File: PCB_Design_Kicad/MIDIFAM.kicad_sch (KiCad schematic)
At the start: 45 parts, among them J1 PWR_IN, J14 Conn_01x07, J15 Conn_01x07, J16 Conn_01x07, J2 ISP connector, U1 TL072, U2 MCP4822, U3 ATmega328, U4 78L05, U5 6N137

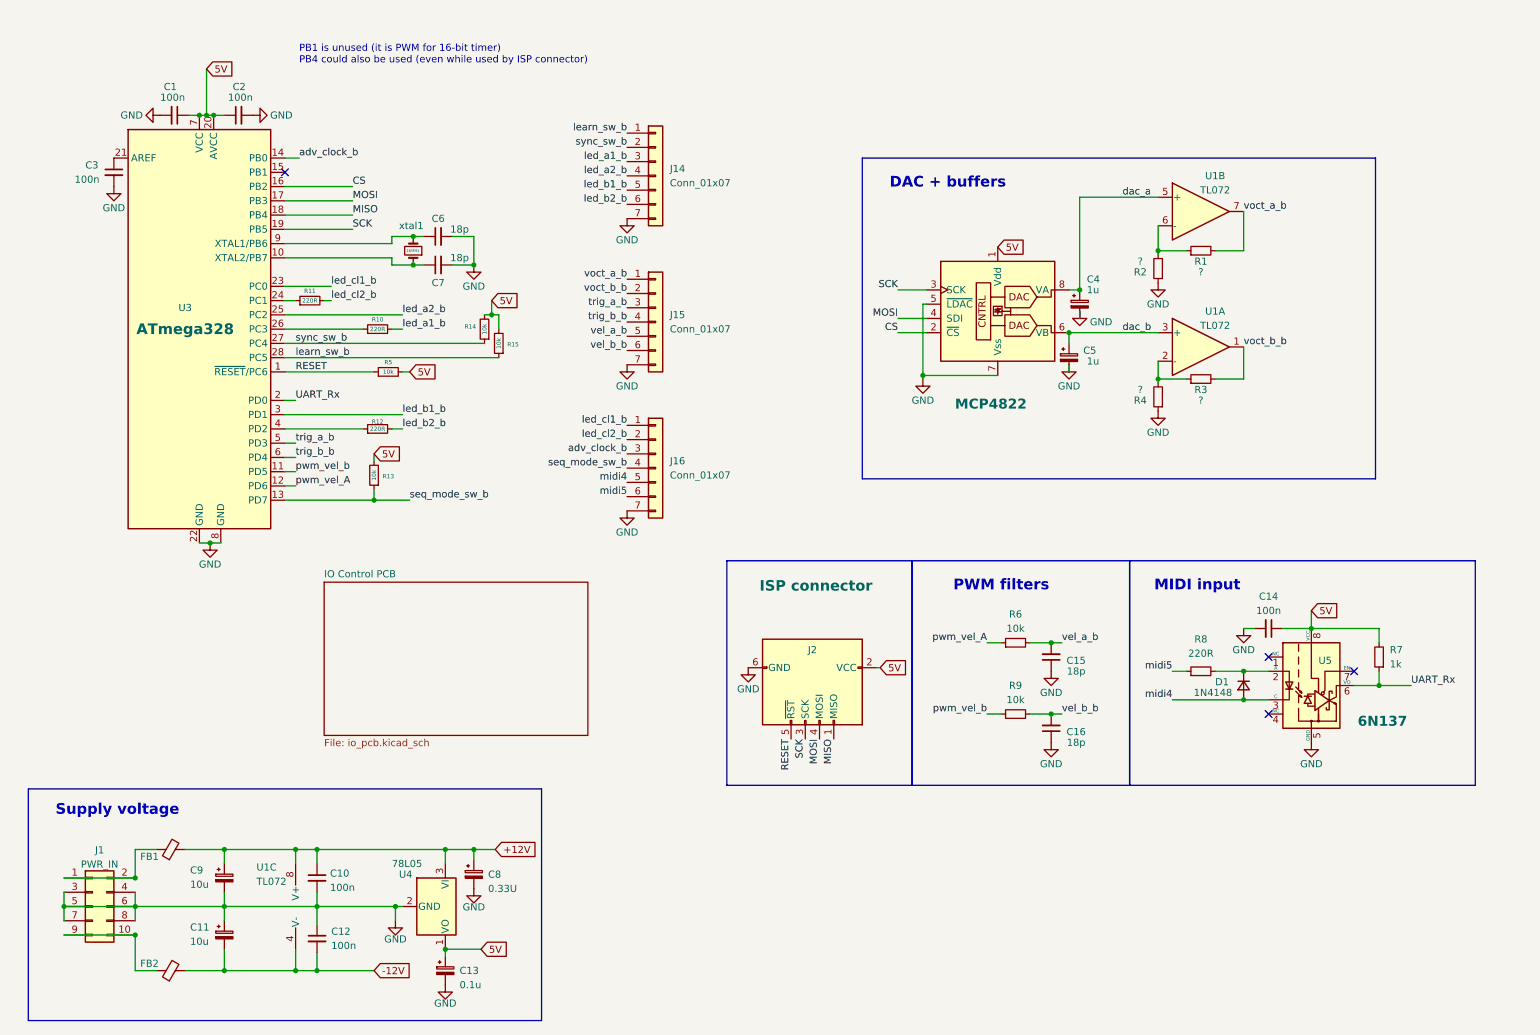
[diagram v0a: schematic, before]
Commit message: SMD pcb, routable and with vias
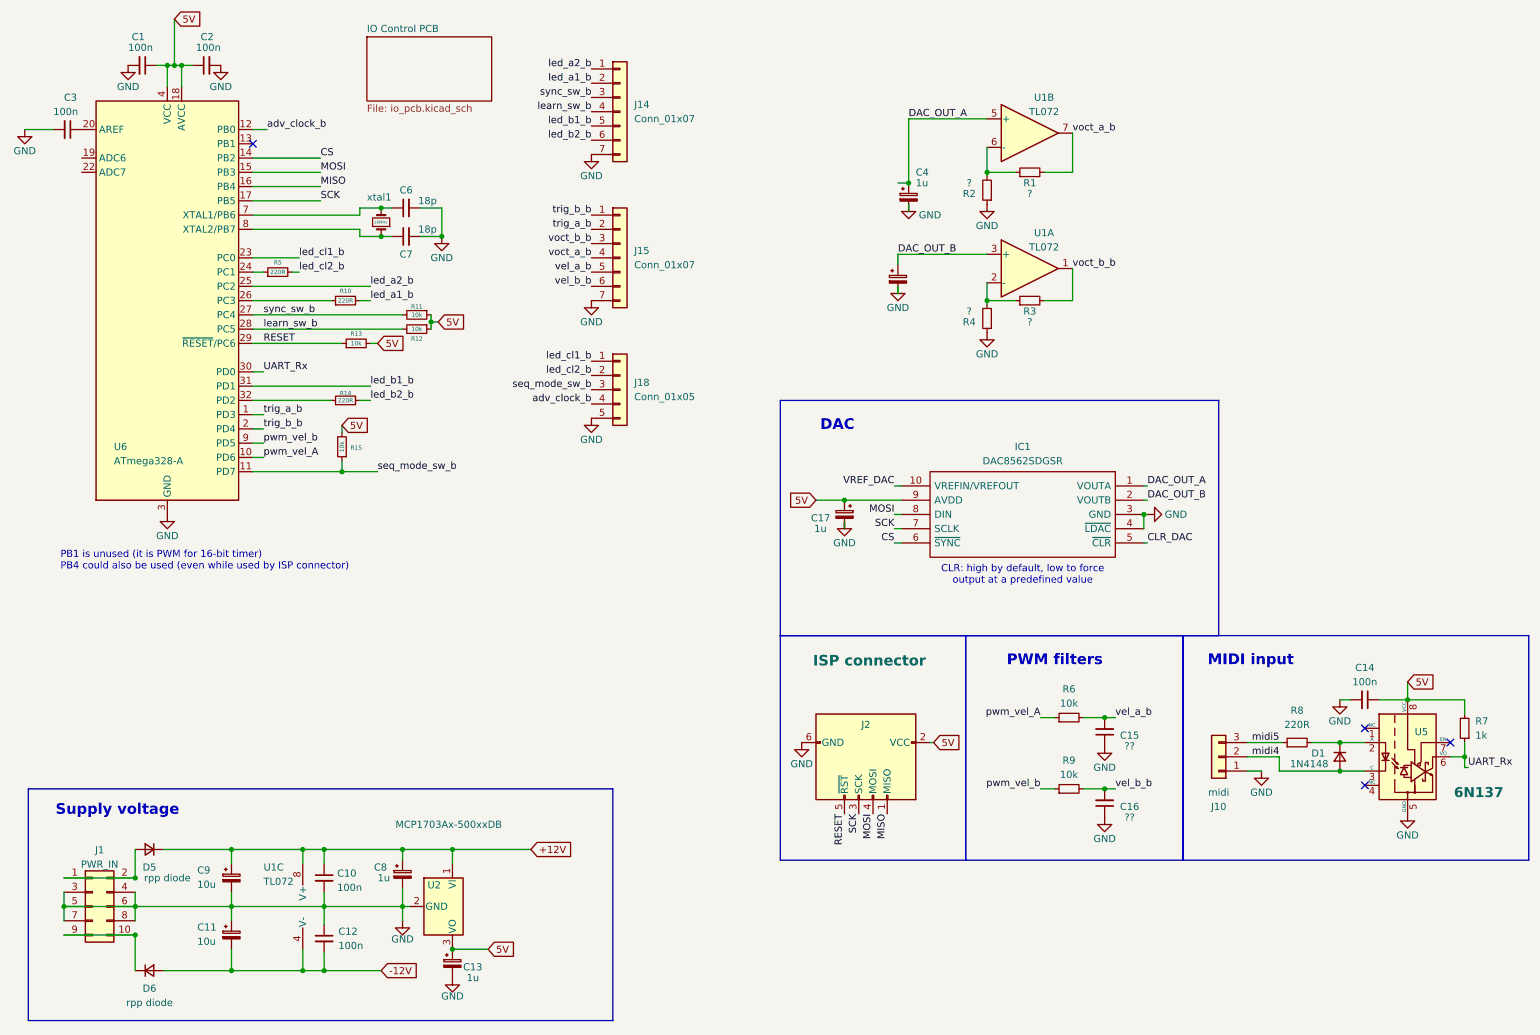
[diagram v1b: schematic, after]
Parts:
- removed FB1, FB2: FerriteBead_Small, Inductor_THT:L_Axial_L5.3mm_D2.2mm_P7.62mm_Horizontal_Vishay_IM-1, symbol Device:FerriteBead_Small
- removed J16: Conn_01x07, Connector_PinHeader_2.54mm:PinHeader_1x07_P2.54mm_Vertical, symbol Connector_Generic:Conn_01x07
- removed U2: MCP4822, Package_DIP:DIP-8_W7.62mm, symbol Analog_DAC:MCP4822
- removed U3: ATmega328, Package_DIP:DIP-28_W7.62mm, symbol MCU_Microchip_ATmega:ATmega328-P
- removed U4: 78L05, Package_TO_SOT_THT:TO-92, symbol Regulator_Linear:L78L05_TO92
- added C17: 1u, Capacitor_SMD:C_0603_1608Metric, symbol Device:C_Polarized_Small
- added D5: rpp diode, Diode_SMD:D_SOD-123F, symbol Device:D_Small
- added D6: rpp diode, Diode_SMD:D_SOD-123, symbol Device:D_Small
- added IC1: DAC8562SDGSR, SamacSys_Parts:SOP50P490X110-10N, symbol SamacSys_Parts:DAC8562SDGSR
- added J10: midi, Connector_PinHeader_2.54mm:PinHeader_1x03_P2.54mm_Vertical, symbol Connector_Generic:Conn_01x03
- added J18: Conn_01x05, Connector_PinHeader_2.54mm:PinHeader_1x05_P2.54mm_Vertical, symbol Connector_Generic:Conn_01x05
- added U2: MCP1703Ax-500xxDB, Package_TO_SOT_SMD:SOT-223-3_TabPin2, symbol Regulator_Linear:MCP1703Ax-500xxDB
- added U6: ATmega328-A, Package_QFP:TQFP-32_7x7mm_P0.8mm, symbol MCU_Microchip_ATmega:ATmega328-A
- C1, C14, C2, C3: footprint Capacitor_THT:C_Disc_D3.0mm_W2.0mm_P2.50mm -> Capacitor_SMD:C_0603_1608Metric
- C10, C12, C6, C7: footprint Capacitor_THT:C_Disc_D3.0mm_W1.6mm_P2.50mm -> Capacitor_SMD:C_0603_1608Metric
- C11, C9: footprint Capacitor_THT:CP_Radial_D5.0mm_P2.50mm -> Capacitor_SMD:CP_Elec_5x5.3
- C13: value 0.1u -> 1u; footprint Capacitor_THT:C_Disc_D3.4mm_W2.1mm_P2.50mm -> Capacitor_SMD:C_0603_1608Metric
- C15, C16: value 18p -> ??; footprint Capacitor_THT:C_Disc_D3.0mm_W1.6mm_P2.50mm -> Capacitor_SMD:C_0603_1608Metric
- C4, C5: footprint Capacitor_THT:C_Disc_D3.8mm_W2.6mm_P2.50mm -> Capacitor_SMD:C_0603_1608Metric
- C8: value 0.33U -> 1u; footprint Capacitor_THT:C_Disc_D3.4mm_W2.1mm_P2.50mm -> Capacitor_SMD:C_0603_1608Metric
- D1: footprint Diode_THT:D_DO-35_SOD27_P2.54mm_Vertical_AnodeUp -> Diode_SMD:D_SOD-323_HandSoldering
- R1, R10, R13, R15, R2, R3, R4, R6, R7, R8, R9: footprint Resistor_THT:R_Axial_DIN0204_L3.6mm_D1.6mm_P2.54mm_Vertical -> Resistor_SMD:R_0603_1608Metric_Pad0.98x0.95mm_HandSolder
- R11, R12: value 220R -> 10k; footprint Resistor_THT:R_Axial_DIN0204_L3.6mm_D1.6mm_P2.54mm_Vertical -> Resistor_SMD:R_0603_1608Metric_Pad0.98x0.95mm_HandSolder
- R14, R5: value 10k -> 220R; footprint Resistor_THT:R_Axial_DIN0204_L3.6mm_D1.6mm_P2.54mm_Vertical -> Resistor_SMD:R_0603_1608Metric_Pad0.98x0.95mm_HandSolder
- U1: footprint Package_DIP:DIP-8_W7.62mm -> Package_SO:SOIC-8_3.9x4.9mm_P1.27mm
- U5: footprint Package_DIP:DIP-8_W7.62mm -> SamacSys_Parts:SOP254P1005X465-8N
- xtal1: footprint CrystalRes:XTAL_HC49P488W46L1150T500H350 -> SamacSys_Parts:XT9M20ANA20M
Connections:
- net +12V: now also D5.1 (K), U2.1 (VI)
- net -12V: now also D6.2 (A)
- net 5V: now also R11.1, R12.1, C17.1, IC1.9 (AVDD), U2.3 (VO), U6.18 (AVCC), U6.4 (VCC), U6.6 (VCC); no longer R14.2, R5.2
- net CS: now also IC1.6 (~{SYNC}), U6.14 (PB2)
- net GND: now also C17.2, IC1.3 (GND), IC1.4 (~{LDAC}), J10.1 (Pin_1), J18.5 (Pin_5), U2.2 (GND), U6.21 (GND), U6.3 (GND), U6.5 (GND)
- net MISO: now also U6.16 (PB4)
- net MOSI: now also IC1.8 (DIN), U6.15 (PB3)
- net RESET: now also R13.1, U6.29 (~{RESET}/PC6); no longer R5.1
- net SCK: now also IC1.7 (SCLK), U6.17 (PB5)
- net UART_Rx: now also U6.30 (PD0)
- net adv_clock_b: now also J18.4 (Pin_4), U6.12 (PB0)
- net learn_sw_b: now also J14.4 (Pin_4), R12.2, U6.28 (PC5); no longer J14.1 (Pin_1), R15.1
- net led_a1_b: now also J14.2 (Pin_2); no longer J14.3 (Pin_3)
- net led_a2_b: now also J14.1 (Pin_1), U6.25 (PC2); no longer J14.4 (Pin_4)
- net led_b1_b: now also U6.31 (PD1)
- net led_b2_b: now also R14.2; no longer R12.2
- net led_cl1_b: now also J18.1 (Pin_1), U6.23 (PC0)
- net led_cl2_b: now also R5.2, J18.2 (Pin_2); no longer R11.2
- net midi4: now also J10.2 (Pin_2)
- net midi5: now also J10.3 (Pin_3)
- net pwm_vel_A: now also U6.10 (PD6)
- net pwm_vel_b: now also U6.9 (PD5)
- net seq_mode_sw_b: now also R15.1, J18.3 (Pin_3), U6.11 (PD7); no longer R13.1
- net sync_sw_b: now also J14.3 (Pin_3), R11.2, U6.27 (PC4); no longer J14.2 (Pin_2), R14.1
- net trig_a_b: now also J15.2 (Pin_2), U6.1 (PD3); no longer J15.3 (Pin_3)
- net trig_b_b: now also J15.1 (Pin_1), U6.2 (PD4); no longer J15.4 (Pin_4)
- net voct_a_b: now also J15.4 (Pin_4); no longer J15.1 (Pin_1)
- net voct_b_b: now also J15.3 (Pin_3); no longer J15.2 (Pin_2)
- net at C7.1, xtal1.1: now also U6.8 (XTAL2/PB7)
- net at C6.1, xtal1.2: now also U6.7 (XTAL1/PB6)
- net at J1.1 (Pin_1), J1.2 (Pin_2): now also D5.2 (A)
- net at J1.10 (Pin_10), J1.9 (Pin_9): now also D6.1 (K)
- net at R10.1: now also U6.26 (PC3)
- net at C3.1: now also U6.20 (AREF)
- net dac_a renamed DAC_OUT_A
- net DAC_OUT_A: now also IC1.1 (VOUTA)
- net dac_b renamed DAC_OUT_B
- net DAC_OUT_B: now also IC1.2 (VOUTB)
- new net: R5.1, U6.24 (PC1)
- new net: R14.1, U6.32 (PD2)
- new net CLR_DAC: IC1.5 (~{CLR})
- new net VREF_DAC: IC1.10 (VREFIN/VREFOUT)
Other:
- note added: "CLR: high by default, low to force output at a predefined value"
- note added: "DAC"
- note removed: "DAC + buffers"
- moved on the sheet: C14, C15, C16, D1, J14, J15, J2, R6, R7, R8, R9, U5

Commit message: routed SMD
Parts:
- removed J14, J15: Conn_01x07, Connector_PinHeader_2.54mm:PinHeader_1x07_P2.54mm_Vertical, symbol Connector_Generic:Conn_01x07
- removed J18: Conn_01x05, Connector_PinHeader_2.54mm:PinHeader_1x05_P2.54mm_Vertical, symbol Connector_Generic:Conn_01x05
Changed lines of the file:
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@@
-	)
-	(symbol
-		(lib_id "Connector_Generic:Conn_01x07")
-		(at 121.92 31.75 0)
-		(unit 1)
-		(exclude_from_sim no)
-		(in_bom yes)
-		(on_board yes)
-		(dnp no)
-		(fields_autoplaced yes)
-		(property "Reference" "J14"
-			(at 124.46 30.4799 0)
-			(effects
-				(font
-					(size 1.27 1.27)
-				)
-				(justify left)
-			)
-		)
-		(property "Value" "Conn_01x07"
-			(at 124.46 33.0199 0)
-			(effects
-				(font
-					(size 1.27 1.27)
-				)
-				(justify left)
-			)
-		)
-		(property "Footprint" "Connector_PinHeader_2.54mm:PinHeader_1x07_P2.54mm_Vertical"
-			(at 121.92 31.75 0)
-			(effects
-				(font
-					(size 1.27 1.27)
-				)
-				(hide yes)
-			)
-		)
-		(property "Datasheet" "~"
-			(at 121.92 31.75 0)
-			(effects
-				(font
-					(size 1.27 1.27)
-				)
-				(hide yes)
-			)
-		)
-		(property "Description" "Generic connector, single row, 01x07, script generated (kicad-library-utils/schlib/autogen/connector/)"
-			(at 121.92 31.75 0)
-			(effects
-				(font
-					(size 1.27 1.27)
-				)
-				(hide yes)
-			)
-		)
-		(pin "6"
-		)
-		(pin "1"
-		)
-		(pin "2"
-		)
-		(pin "3"
-		)
-		(pin "7"
-		)
-		(pin "5"
-		)
-		(pin "4"
-		)
-		(instances
-			(project "MIDIFAM"
-				(path "/4d4d84f1-a7a8-42a8-95d1-cf69d5b591e2"
-					(reference "J14")
-					(unit 1)
-				)
-			)
-		)
 	)
 	(symbol
@@
 	)
 	(symbol
-		(lib_id "Connector_Generic:Conn_01x07")
-		(at 121.92 57.785 0)
-		(unit 1)
-		(exclude_from_sim no)
-		(in_bom yes)
-		(on_board yes)
-		(dnp no)
-		(fields_autoplaced yes)
-		(property "Reference" "J15"
-			(at 124.46 56.5149 0)
-			(effects
-				(font
-					(size 1.27 1.27)
-				)
-				(justify left)
-			)
-		)
-		(property "Value" "Conn_01x07"
-			(at 124.46 59.0549 0)
-			(effects
-				(font
-					(size 1.27 1.27)
-				)
-				(justify left)
-			)
-		)
-		(property "Footprint" "Connector_PinHeader_2.54mm:PinHeader_1x07_P2.54mm_Vertical"
-			(at 121.92 57.785 0)
-			(effects
-				(font
-					(size 1.27 1.27)
-				)
-				(hide yes)
-			)
-		)
-		(property "Datasheet" "~"
-			(at 121.92 57.785 0)
-			(effects
-				(font
-					(size 1.27 1.27)
-				)
-				(hide yes)
-			)
-		)
-		(property "Description" "Generic connector, single row, 01x07, script generated (kicad-library-utils/schlib/autogen/connector/)"
-			(at 121.92 57.785 0)
-			(effects
-				(font
-					(size 1.27 1.27)
-				)
-				(hide yes)
-			)
-		)
-		(pin "6"
-		)
-		(pin "1"
-		)
-		(pin "2"
-		)
-		(pin "3"
-		)
-		(pin "7"
-		)
-		(pin "5"
-		)
-		(pin "4"
-		)
-		(instances
-			(project "MIDIFAM"
-				(path "/4d4d84f1-a7a8-42a8-95d1-cf69d5b591e2"
-					(reference "J15")
-					(unit 1)
-				)
-			)
-		)
-	)
-	(symbol
 		(lib_id "Amplifier_Operational:TL072")
 		(at 67.945 173.355 0)
@@
 				)
 			)
-		)
-	)
-	(symbol
-		(lib_id "Connector_Generic:Conn_01x05")
-		(at 121.92 81.28 0)
-		(unit 1)
-		(exclude_from_sim no)
-		(in_bom yes)
-		(on_board yes)
-		(dnp no)
-		(fields_autoplaced yes)
-		(property "Reference" "J18"
-			(at 124.46 80.0099 0)
-			(effects
-				(font
-					(size 1.27 1.27)
-				)
-				(justify left)
-			)
-		)
-		(property "Value" "Conn_01x05"
-			(at 124.46 82.5499 0)
-			(effects
-				(font
-					(size 1.27 1.27)
-				)
-				(justify left)
-			)
-		)
-		(property "Footprint" "Connector_PinHeader_2.54mm:PinHeader_1x05_P2.54mm_Vertical"
-			(at 121.92 81.28 0)
-			(effects
-				(font
-					(size 1.27 1.27)
-				)
-				(hide yes)
-			)
-		)
-		(property "Datasheet" "~"
-			(at 121.92 81.28 0)
-			(effects
-				(font
-					(size 1.27 1.27)
-				)
-				(hide yes)
-			)
-		)
-		(property "Description" "Generic connector, single row, 01x05, script generated (kicad-library-utils/schlib/autogen/connector/)"
-			(at 121.92 81.28 0)
-			(effects
-				(font
-					(size 1.27 1.27)
-				)
-				(hide yes)
-			)
-		)
-		(pin "1"
-		)
-		(pin "5"
-		)
-		(pin "2"
-		)
-		(pin "4"
-		)
-		(pin "3"
-		)
-		(instances
-			(project ""
-				(path "/4d4d84f1-a7a8-42a8-95d1-cf69d5b591e2"
-					(reference "J18")
-					(unit 1)
-				)
-			)
